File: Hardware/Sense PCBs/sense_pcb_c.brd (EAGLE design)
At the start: 17.5 x 233 mm, 29 parts, among them J1 DF11-16DP-2DSA(01)

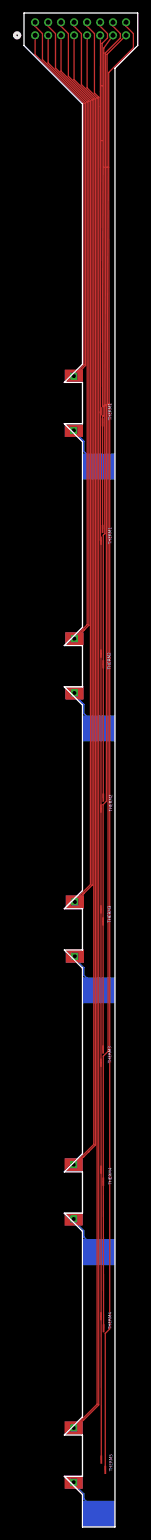
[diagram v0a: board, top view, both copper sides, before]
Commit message: fixed outline, updated gerbers
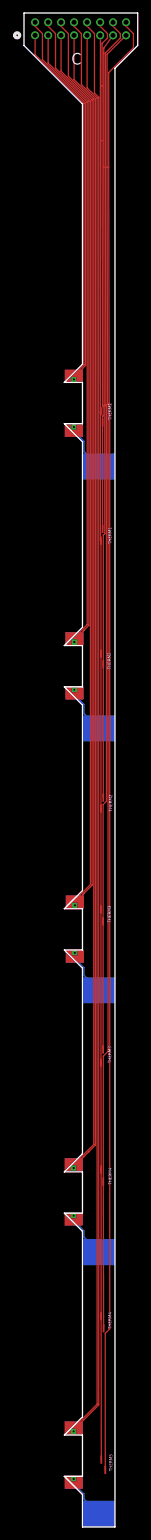
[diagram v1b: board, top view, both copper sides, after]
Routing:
- net N$10: track 275.0 -> 275.8 mm
- net N$3: track 114.7 -> 115.5 mm
- net N$11: track 194.9 -> 195.8 mm
- net N$7: track 435.2 -> 436.1 mm
- net N$1: track 355.1 -> 355.9 mm
- net N$8: track 7.02 -> 7.53 mm
- net N$6: track 6.78 -> 7.28 mm
- net N$5: track 7.16 -> 7.67 mm
- net N$4: track 6.71 -> 7.22 mm
- net N$2: track 6.45 -> 6.95 mm
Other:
- board text added: "C"
